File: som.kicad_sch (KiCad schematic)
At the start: 35 parts, among them J15 Bus_DDR4_SODIMM_CUSTOM_Jetson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, U4 NTS0102

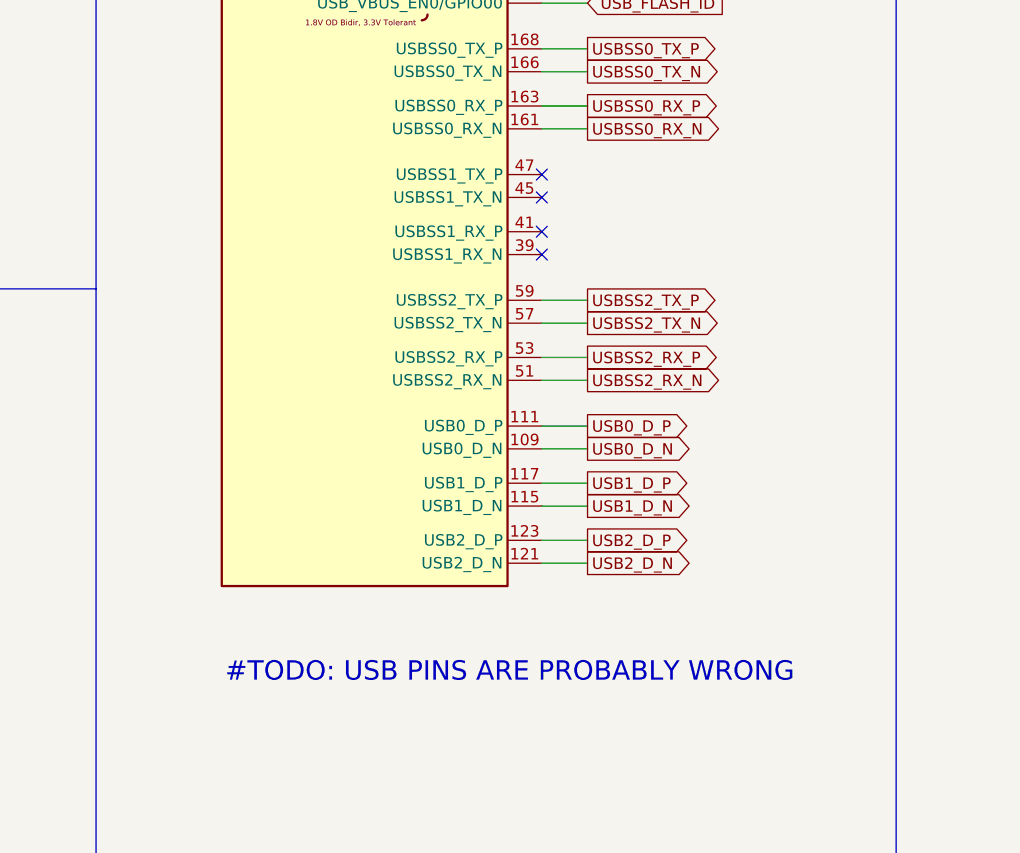
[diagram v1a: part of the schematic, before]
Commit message: Finish HDMI routing, replace usbc w/ usba
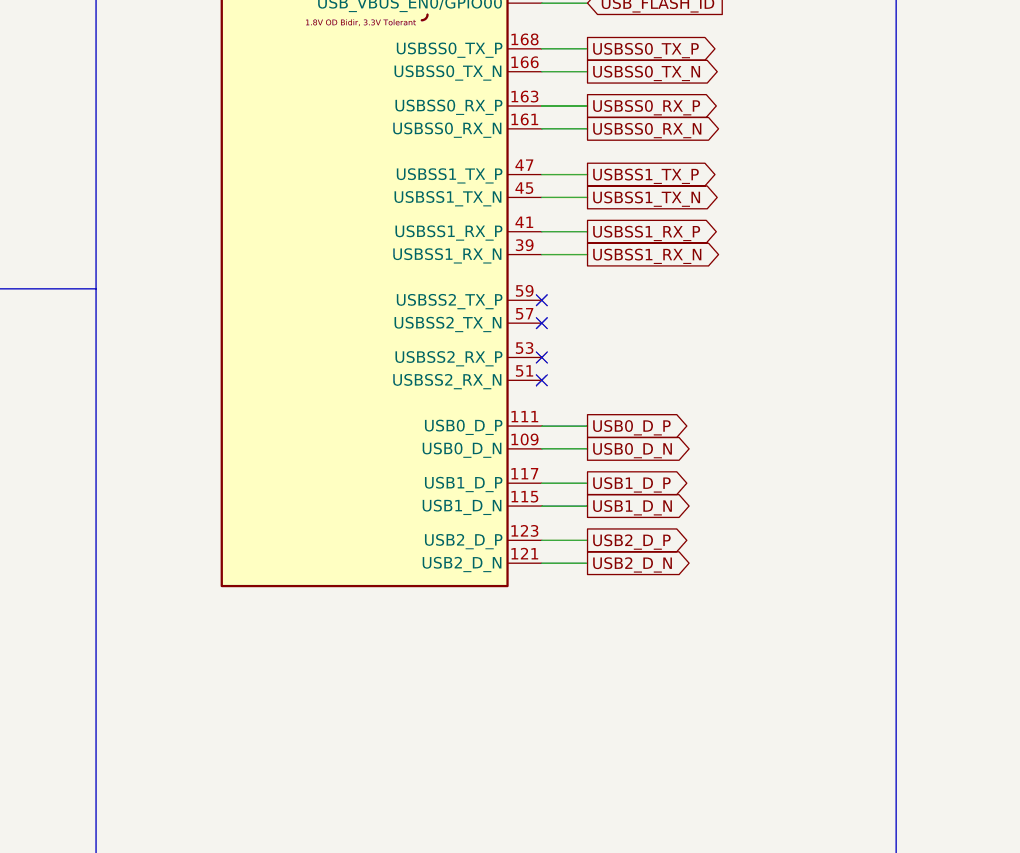
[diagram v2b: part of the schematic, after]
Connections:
- net USBSS1_RX_N: now reaches J15.39 (USBSS1_RX_N)
- net USBSS1_RX_P: now reaches J15.41 (USBSS1_RX_P)
- net USBSS1_TX_N: now reaches J15.45 (USBSS1_TX_N)
- net USBSS1_TX_P: now reaches J15.47 (USBSS1_TX_P)
- net USBSS2_RX_N: no longer names the net of J15.51 (USBSS2_RX_N)
- net USBSS2_RX_P: no longer names the net of J15.53 (USBSS2_RX_P)
- net USBSS2_TX_N: no longer names the net of J15.57 (USBSS2_TX_N)
- net USBSS2_TX_P: no longer names the net of J15.59 (USBSS2_TX_P)
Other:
- note removed: "#TODO: USB PINS ARE PROBABLY WRONG"
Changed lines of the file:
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@@
 		)
 	)
-	(text "#TODO: USB PINS ARE PROBABLY WRONG"
-		(exclude_from_sim no)
-		(at 185.674 261.112 0)
-		(effects
-			(font
-				(size 2.159 2.159)
-			)
-		)
-	)
 	(text "Miscellaneous"
 		(exclude_from_sim no)
@@
 	)
 	(no_connect
-		(at 189.23 208.28)
+		(at 189.23 222.25)
 	)
 	(no_connect
@@
 	)
 	(no_connect
-		(at 189.23 214.63)
+		(at 189.23 228.6)
 	)
 	(no_connect
@@
 	)
 	(no_connect
-		(at 189.23 205.74)
+		(at 189.23 219.71)
 	)
 	(no_connect
@@
 	)
 	(no_connect
-		(at 189.23 212.09)
+		(at 189.23 226.06)
 	)
 	(no_connect
@@
 	(wire
 		(pts
-			(xy 189.23 228.6) (xy 194.31 228.6)
+			(xy 189.23 214.63) (xy 194.31 214.63)
 		)
 		(stroke
@@
 	(wire
 		(pts
-			(xy 189.23 219.71) (xy 194.31 219.71)
+			(xy 189.23 205.74) (xy 194.31 205.74)
 		)
 		(stroke
@@
 	(wire
 		(pts
-			(xy 189.23 226.06) (xy 194.31 226.06)
+			(xy 189.23 212.09) (xy 194.31 212.09)
 		)
 		(stroke
@@
 	(wire
 		(pts
-			(xy 189.23 222.25) (xy 194.31 222.25)
+			(xy 189.23 208.28) (xy 194.31 208.28)
 		)
 		(stroke
@@
 		)
 	)
-	(global_label "USBSS2_RX_P"
+	(global_label "USBSS1_RX_P"
 		(shape output)
-		(at 194.31 226.06 0)
+		(at 194.31 212.09 0)
 		(effects
 			(font
@@
 		)
 		(property "Intersheetrefs" "${INTERSHEET_REFS}"
-			(at 210.185 226.06 0)
+			(at 210.185 212.09 0)
 			(show_name no)
 			(do_not_autoplace no)
@@
 		)
 	)
-	(global_label "USBSS2_TX_P"
+	(global_label "USBSS1_TX_P"
 		(shape output)
-		(at 194.31 219.71 0)
+		(at 194.31 205.74 0)
 		(effects
 			(font
@@
 		)
 		(property "Intersheetrefs" "${INTERSHEET_REFS}"
-			(at 210.185 219.71 0)
+			(at 210.185 205.74 0)
 			(show_name no)
 			(do_not_autoplace no)
@@
 		)
 	)
-	(global_label "USBSS2_TX_N"
+	(global_label "USBSS1_TX_N"
 		(shape output)
-		(at 194.31 222.25 0)
+		(at 194.31 208.28 0)
 		(effects
 			(font
@@
 		)
 		(property "Intersheetrefs" "${INTERSHEET_REFS}"
-			(at 210.185 222.25 0)
+			(at 210.185 208.28 0)
 			(show_name no)
 			(do_not_autoplace no)
@@
 		)
 	)
-	(global_label "USBSS2_RX_N"
+	(global_label "USBSS1_RX_N"
 		(shape output)
-		(at 194.31 228.6 0)
+		(at 194.31 214.63 0)
 		(effects
 			(font
@@
 		)
 		(property "Intersheetrefs" "${INTERSHEET_REFS}"
-			(at 210.185 228.6 0)
+			(at 210.185 214.63 0)
 			(show_name no)
 			(do_not_autoplace no)
